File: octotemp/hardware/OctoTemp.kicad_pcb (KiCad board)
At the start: 2 copper layers, 47.2 x 34 mm, 48 parts, among them U1 ESP-12E, U2 SPX3819M5, U3 ADC128D818

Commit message: Added name/version silkscreening.
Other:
- board text added: "z2amiller OctoTemp v0.2.1"
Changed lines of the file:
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@@
     (links 100)
     (no_connects 0)
-    (area 15.514536 18.70288 75.926201 59.0464)
+    (area 20.674999 20.502999 68.075001 54.653001)
     (thickness 1.6)
-    (drawings 4)
+    (drawings 5)
     (tracks 219)
     (zones 0)
@@
     (fp_circle (center 0 0) (end 2.5 0) (layer Cmts.User) (width 0.381))
     (pad 1 thru_hole circle (at 0 0) (size 2.5 2.5) (drill 2.5) (layers))
+  )
+  (gr_text "z2amiller OctoTemp v0.2.1" (at 66.55 36.328 90) (layer B.SilkS)
+    (effects (font (size 1.5 1.5) (thickness 0.3)) (justify mirror))
   )
   (gr_line (start 68 20.578) (end 68 54.578) (angle 90) (layer Edge.Cuts) (width 0.15))
@@
   (segment (start 53.75 45.828) (end 53.75 46.078) (width 0.25) (layer F.Cu) (net 3))
   (segment (start 53.75 46.078) (end 47.75 52.078) (width 0.25) (layer F.Cu) (net 3))
-  (segment (start 48.055 36.457) (end 49.198 36.457) (width 0.25) (layer F.Cu) (net 4) (status 400000))
-  (segment (start 67.25 38.888) (end 67.25 42.078) (width 0.25) (layer F.Cu) (net 4) (status 800000))
+  (segment (start 48.055 36.457) (end 49.198 36.457) (width 0.25) (layer F.Cu) (net 4))
+  (segment (start 67.25 38.888) (end 67.25 42.078) (width 0.25) (layer F.Cu) (net 4))
   (segment (start 64.438 36.076) (end 67.25 38.888) (width 0.25) (layer F.Cu) (net 4))
   (segment (start 49.579 36.076) (end 64.438 36.076) (width 0.25) (layer F.Cu) (net 4))
@@
   (segment (start 57.5 40.328) (end 46.75 40.328) (width 0.25) (layer B.Cu) (net 6))
   (segment (start 59.25 42.078) (end 57.5 40.328) (width 0.25) (layer B.Cu) (net 6))
-  (segment (start 61.25 26.078) (end 61.25 26.411) (width 0.25) (layer F.Cu) (net 7) (status C00000))
-  (segment (start 61.25 26.411) (end 63.041 28.202) (width 0.25) (layer F.Cu) (net 7) (status 400000))
-  (segment (start 65.708 28.202) (end 67.25 26.66) (width 0.25) (layer F.Cu) (net 7) (status 800000))
+  (segment (start 61.25 26.078) (end 61.25 26.411) (width 0.25) (layer F.Cu) (net 7))
+  (segment (start 61.25 26.411) (end 63.041 28.202) (width 0.25) (layer F.Cu) (net 7))
+  (segment (start 65.708 28.202) (end 67.25 26.66) (width 0.25) (layer F.Cu) (net 7))
   (segment (start 63.041 28.202) (end 65.708 28.202) (width 0.25) (layer F.Cu) (net 7))
-  (segment (start 67.25 26.66) (end 67.25 26.078) (width 0.25) (layer F.Cu) (net 7) (status C00000))
-  (segment (start 45.515 41.537) (end 46.785 40.267) (width 0.25) (layer F.Cu) (net 7) (status 400000))
-  (segment (start 61.25 30.755) (end 61.25 26.078) (width 0.25) (layer F.Cu) (net 7) (status 800000))
+  (segment (start 67.25 26.66) (end 67.25 26.078) (width 0.25) (layer F.Cu) (net 7))
+  (segment (start 45.515 41.537) (end 46.785 40.267) (width 0.25) (layer F.Cu) (net 7))
+  (segment (start 61.25 30.755) (end 61.25 26.078) (width 0.25) (layer F.Cu) (net 7))
   (segment (start 57.961 34.044) (end 61.25 30.755) (width 0.25) (layer F.Cu) (net 7))
   (segment (start 55.294 34.044) (end 57.961 34.044) (width 0.25) (layer F.Cu) (net 7))

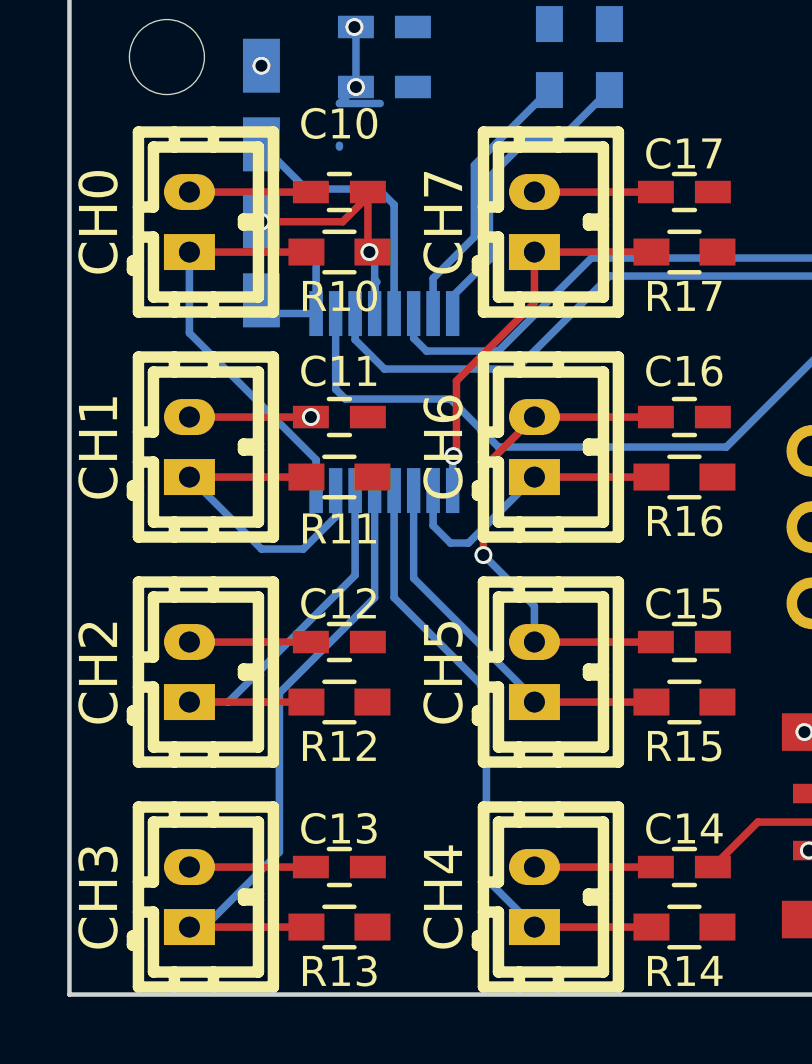
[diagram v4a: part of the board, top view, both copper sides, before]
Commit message: Increased the drill sizes of the JST connectors
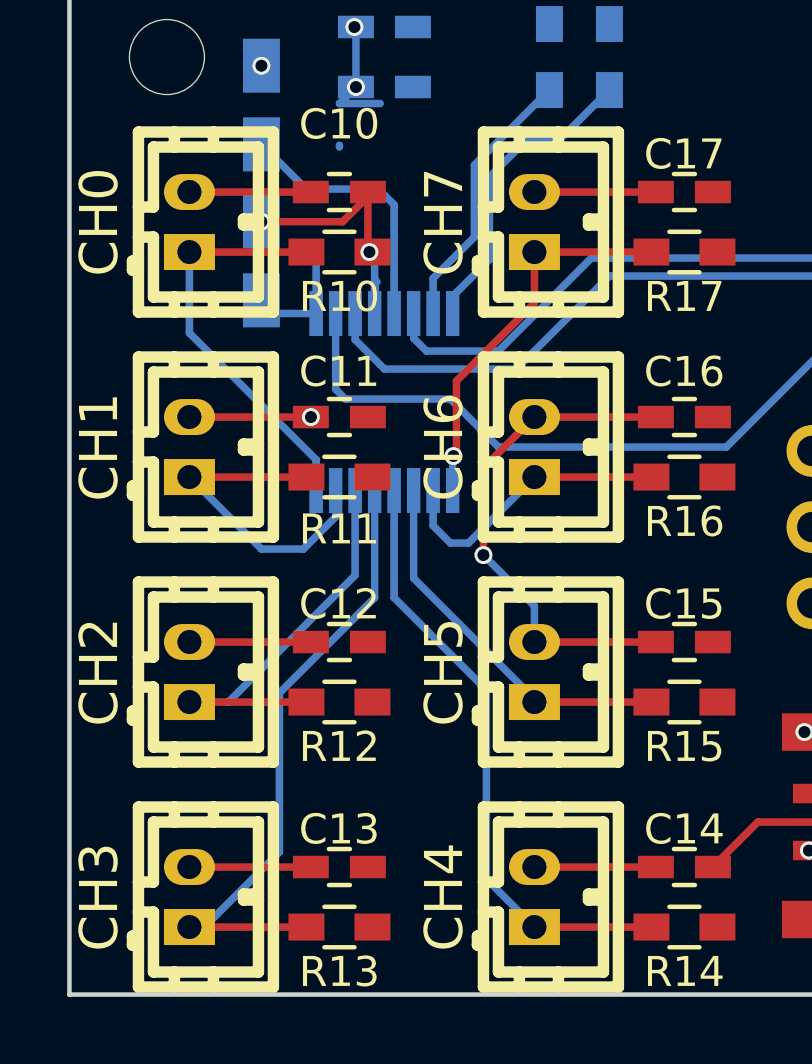
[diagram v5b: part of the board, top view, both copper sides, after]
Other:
- board text added: "z2amiller OctoTemp v0.2.2"
- board text removed: "z2amiller OctoTemp v0.2.1"
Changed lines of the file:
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@@
-(kicad_pcb (version 4) (host pcbnew "(2015-10-28 BZR 6285)-product")
+(kicad_pcb (version 4) (host pcbnew "(2016-01-28 BZR 6518)-product")
   (general
     (links 100)
     (no_connects 0)
-    (area 20.674999 20.502999 68.075001 54.653001)
+    (area 15.514536 18.70288 75.926201 59.0464)
     (thickness 1.6)
     (drawings 5)
@@
     (mod_text_size 1 1)
     (mod_text_width 0.15)
-    (pad_size 1.524 1.524)
-    (pad_drill 0.762)
+    (pad_size 1.19888 1.69926)
+    (pad_drill 0.80104)
     (pad_to_mask_clearance 0.2)
     (aux_axis_origin 0 0)
     (grid_origin 20.75 20.328)
-    (visible_elements FFFFFF7F)
+    (visible_elements FFFEFF7F)
     (pcbplotparams
       (layerselection 0x010f0_80000001)
@@
     (fp_line (start 2.99974 -1.69926) (end -2.99974 -1.69926) (layer F.SilkS) (width 0.381))
     (fp_line (start -2.99974 2.79908) (end 2.99974 2.79908) (layer F.SilkS) (width 0.381))
-    (pad 1 thru_hole rect (at -1.00076 0 90) (size 1.19888 1.69926) (drill 0.70104) (layers *.Cu *.Mask F.SilkS)
+    (pad 1 thru_hole rect (at -1.00076 0 90) (size 1.19888 1.69926) (drill 0.80104) (layers *.Cu *.Mask F.SilkS)
       (net 8 IN0))
-    (pad 2 thru_hole oval (at 1.00076 0 90) (size 1.19888 1.69926) (drill 0.70104) (layers *.Cu *.Mask F.SilkS)
+    (pad 2 thru_hole oval (at 1.00076 0 90) (size 1.19888 1.69926) (drill 0.80104) (layers *.Cu *.Mask F.SilkS)
       (net 1 ADC_VIN))
     (model walter/conn_jst-ph/b2b-ph-kl.wrl
@@
     (fp_line (start 2.99974 -1.69926) (end -2.99974 -1.69926) (layer F.SilkS) (width 0.381))
     (fp_line (start -2.99974 2.79908) (end 2.99974 2.79908) (layer F.SilkS) (width 0.381))
-    (pad 1 thru_hole rect (at -1.00076 0 90) (size 1.19888 1.69926) (drill 0.70104) (layers *.Cu *.Mask F.SilkS)
+    (pad 1 thru_hole rect (at -1.00076 0 90) (size 1.19888 1.69926) (drill 0.80104) (layers *.Cu *.Mask F.SilkS)
       (net 9 IN1))
-    (pad 2 thru_hole oval (at 1.00076 0 90) (size 1.19888 1.69926) (drill 0.70104) (layers *.Cu *.Mask F.SilkS)
+    (pad 2 thru_hole oval (at 1.00076 0 90) (size 1.19888 1.69926) (drill 0.80104) (layers *.Cu *.Mask F.SilkS)
       (net 1 ADC_VIN))
     (model walter/conn_jst-ph/b2b-ph-kl.wrl
@@
     (fp_line (start 2.99974 -1.69926) (end -2.99974 -1.69926) (layer F.SilkS) (width 0.381))
     (fp_line (start -2.99974 2.79908) (end 2.99974 2.79908) (layer F.SilkS) (width 0.381))
-    (pad 1 thru_hole rect (at -1.00076 0 90) (size 1.19888 1.69926) (drill 0.70104) (layers *.Cu *.Mask F.SilkS)
+    (pad 1 thru_hole rect (at -1.00076 0 90) (size 1.19888 1.69926) (drill 0.80104) (layers *.Cu *.Mask F.SilkS)
       (net 10 IN2))
-    (pad 2 thru_hole oval (at 1.00076 0 90) (size 1.19888 1.69926) (drill 0.70104) (layers *.Cu *.Mask F.SilkS)
+    (pad 2 thru_hole oval (at 1.00076 0 90) (size 1.19888 1.69926) (drill 0.80104) (layers *.Cu *.Mask F.SilkS)
       (net 1 ADC_VIN))
     (model walter/conn_jst-ph/b2b-ph-kl.wrl
@@
     (fp_line (start 2.99974 -1.69926) (end -2.99974 -1.69926) (layer F.SilkS) (width 0.381))
     (fp_line (start -2.99974 2.79908) (end 2.99974 2.79908) (layer F.SilkS) (width 0.381))
-    (pad 1 thru_hole rect (at -1.00076 0 90) (size 1.19888 1.69926) (drill 0.70104) (layers *.Cu *.Mask F.SilkS)
+    (pad 1 thru_hole rect (at -1.00076 0 90) (size 1.19888 1.69926) (drill 0.80104) (layers *.Cu *.Mask F.SilkS)
       (net 11 IN3))
-    (pad 2 thru_hole oval (at 1.00076 0 90) (size 1.19888 1.69926) (drill 0.70104) (layers *.Cu *.Mask F.SilkS)
+    (pad 2 thru_hole oval (at 1.00076 0 90) (size 1.19888 1.69926) (drill 0.80104) (layers *.Cu *.Mask F.SilkS)
       (net 1 ADC_VIN))
     (model walter/conn_jst-ph/b2b-ph-kl.wrl
@@
     (fp_line (start 2.99974 -1.69926) (end -2.99974 -1.69926) (layer F.SilkS) (width 0.381))
     (fp_line (start -2.99974 2.79908) (end 2.99974 2.79908) (layer F.SilkS) (width 0.381))
-    (pad 1 thru_hole rect (at -1.00076 0 90) (size 1.19888 1.69926) (drill 0.70104) (layers *.Cu *.Mask F.SilkS)
+    (pad 1 thru_hole rect (at -1.00076 0 90) (size 1.19888 1.69926) (drill 0.80104) (layers *.Cu *.Mask F.SilkS)
       (net 12 IN4))
-    (pad 2 thru_hole oval (at 1.00076 0 90) (size 1.19888 1.69926) (drill 0.70104) (layers *.Cu *.Mask F.SilkS)
+    (pad 2 thru_hole oval (at 1.00076 0 90) (size 1.19888 1.69926) (drill 0.80104) (layers *.Cu *.Mask F.SilkS)
       (net 1 ADC_VIN))
     (model walter/conn_jst-ph/b2b-ph-kl.wrl
@@
     (fp_line (start 2.99974 -1.69926) (end -2.99974 -1.69926) (layer F.SilkS) (width 0.381))
     (fp_line (start -2.99974 2.79908) (end 2.99974 2.79908) (layer F.SilkS) (width 0.381))
-    (pad 1 thru_hole rect (at -1.00076 0 90) (size 1.19888 1.69926) (drill 0.70104) (layers *.Cu *.Mask F.SilkS)
+    (pad 1 thru_hole rect (at -1.00076 0 90) (size 1.19888 1.69926) (drill 0.80104) (layers *.Cu *.Mask F.SilkS)
       (net 13 IN5))
-    (pad 2 thru_hole oval (at 1.00076 0 90) (size 1.19888 1.69926) (drill 0.70104) (layers *.Cu *.Mask F.SilkS)
+    (pad 2 thru_hole oval (at 1.00076 0 90) (size 1.19888 1.69926) (drill 0.80104) (layers *.Cu *.Mask F.SilkS)
       (net 1 ADC_VIN))
     (model walter/conn_jst-ph/b2b-ph-kl.wrl
@@
     (fp_line (start 2.99974 -1.69926) (end -2.99974 -1.69926) (layer F.SilkS) (width 0.381))
     (fp_line (start -2.99974 2.79908) (end 2.99974 2.79908) (layer F.SilkS) (width 0.381))
-    (pad 1 thru_hole rect (at -1.00076 0 90) (size 1.19888 1.69926) (drill 0.70104) (layers *.Cu *.Mask F.SilkS)
+    (pad 1 thru_hole rect (at -1.00076 0 90) (size 1.19888 1.69926) (drill 0.80104) (layers *.Cu *.Mask F.SilkS)
       (net 14 IN6))
-    (pad 2 thru_hole oval (at 1.00076 0 90) (size 1.19888 1.69926) (drill 0.70104) (layers *.Cu *.Mask F.SilkS)
+    (pad 2 thru_hole oval (at 1.00076 0 90) (size 1.19888 1.69926) (drill 0.80104) (layers *.Cu *.Mask F.SilkS)
       (net 1 ADC_VIN))
     (model walter/conn_jst-ph/b2b-ph-kl.wrl
@@
     (fp_line (start 2.99974 -1.69926) (end -2.99974 -1.69926) (layer F.SilkS) (width 0.381))
     (fp_line (start -2.99974 2.79908) (end 2.99974 2.79908) (layer F.SilkS) (width 0.381))
-    (pad 1 thru_hole rect (at -1.00076 0 90) (size 1.19888 1.69926) (drill 0.70104) (layers *.Cu *.Mask F.SilkS)
+    (pad 1 thru_hole rect (at -1.00076 0 90) (size 1.19888 1.69926) (drill 0.80104) (layers *.Cu *.Mask F.SilkS)
       (net 15 IN7))
-    (pad 2 thru_hole oval (at 1.00076 0 90) (size 1.19888 1.69926) (drill 0.70104) (layers *.Cu *.Mask F.SilkS)
+    (pad 2 thru_hole oval (at 1.00076 0 90) (size 1.19888 1.69926) (drill 0.80104) (layers *.Cu *.Mask F.SilkS)
       (net 1 ADC_VIN))
     (model walter/conn_jst-ph/b2b-ph-kl.wrl
@@
     (pad 1 thru_hole circle (at 0 0) (size 2.5 2.5) (drill 2.5) (layers))
   )
-  (gr_text "z2amiller OctoTemp v0.2.1" (at 66.55 36.328 90) (layer B.SilkS)
+  (gr_text "z2amiller OctoTemp v0.2.2" (at 66.55 36.328 90) (layer B.SilkS)
     (effects (font (size 1.5 1.5) (thickness 0.3)) (justify mirror))
   )
